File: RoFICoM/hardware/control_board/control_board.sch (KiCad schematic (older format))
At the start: 27 parts, among them J1 Skirt Cable, J2 M+, J3 M-, J4 SWD, J5 DBG_UART, J6 SYS_CON, J7 SLIDER, U1 STM32G071GBU6, U2 DRV8837C, U3 BU52272NUZ, U4 MIC5365, U5 BU52272NUZ

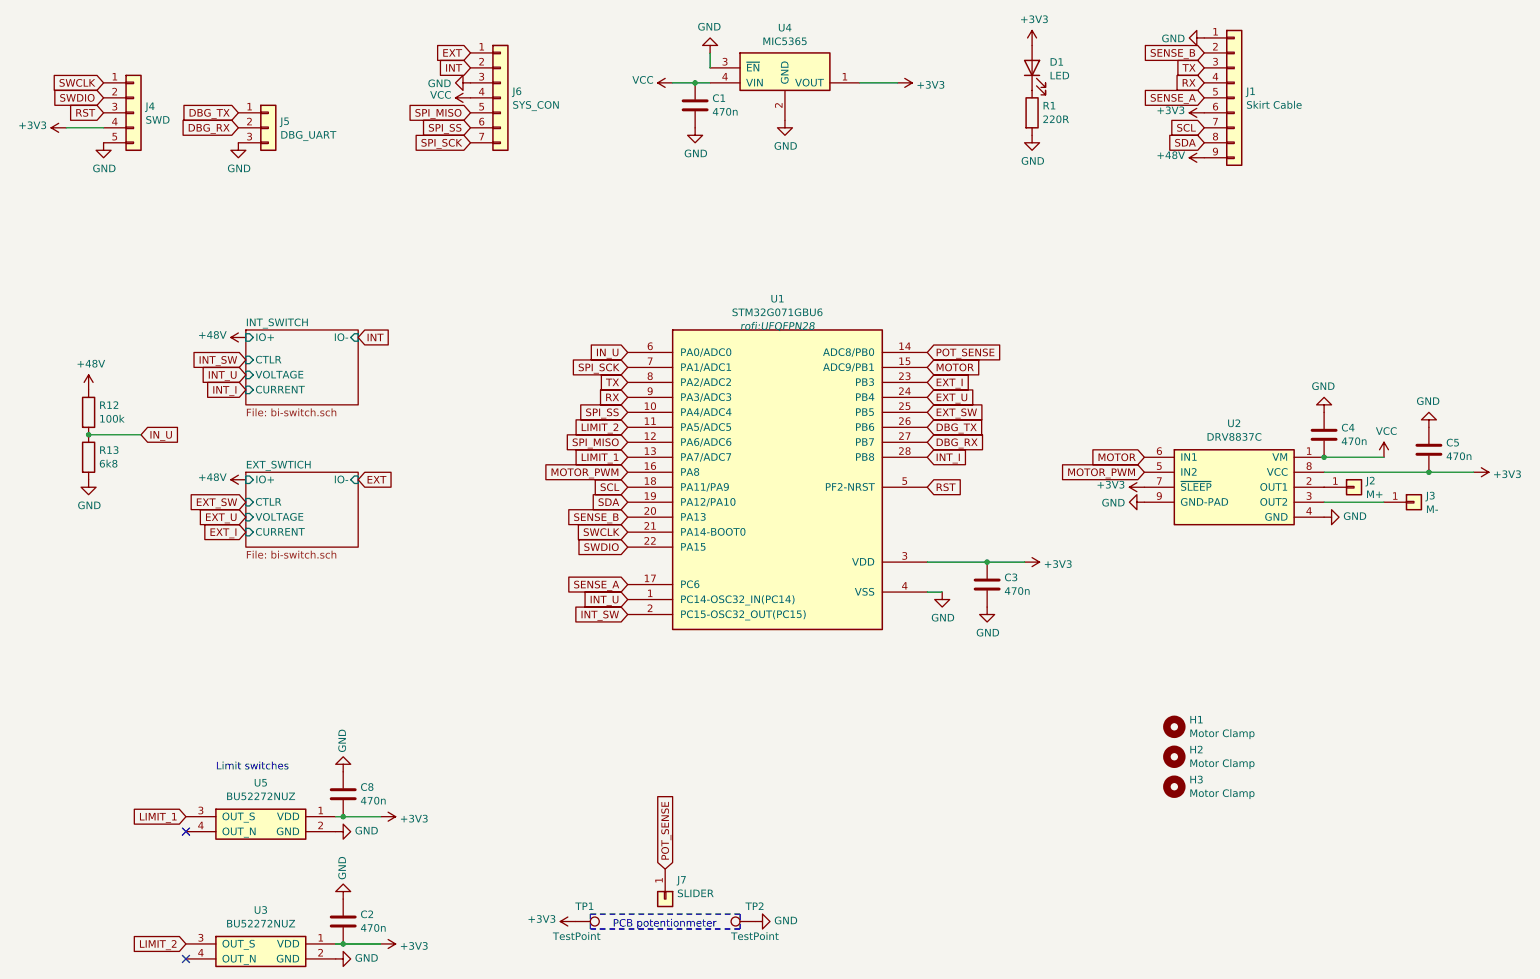
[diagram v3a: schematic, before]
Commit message: RoFICoM: Add new board revision
- change voltage regulator and switching transistors
- fix wrong wiring of SWD
- add Molex board-to-board connectors for system and debugging
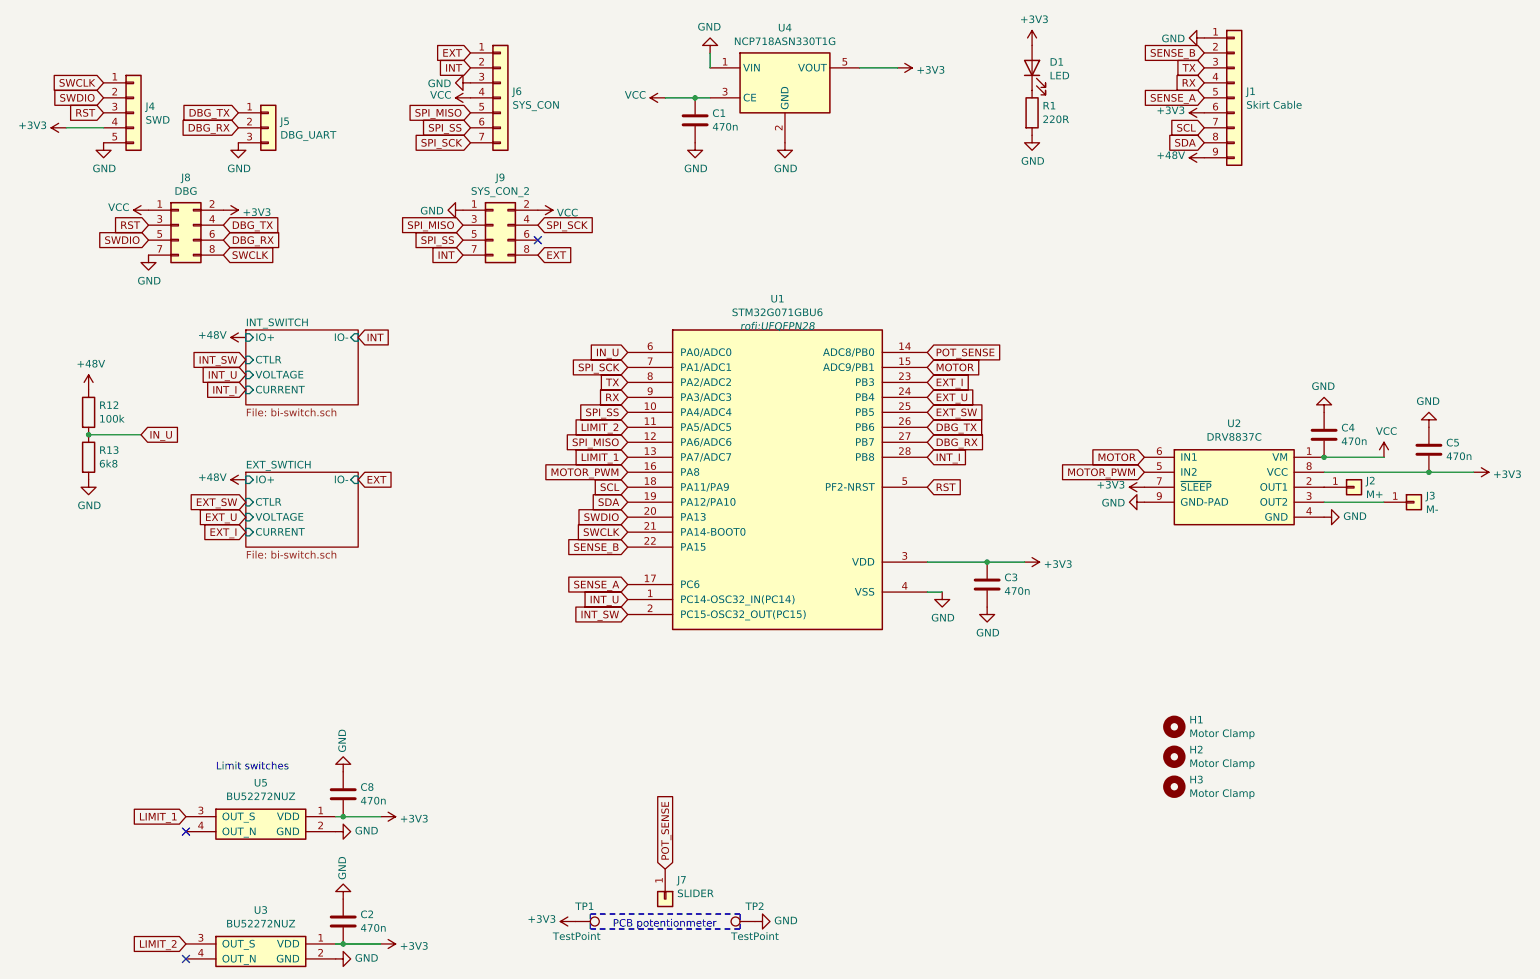
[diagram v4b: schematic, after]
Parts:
- removed U4: MIC5365, rofi:MLF-4, symbol rofi:MIC5365
- added J8: DBG, rofi:molex-505006-0812, symbol Connector_Generic:Conn_02x04_Odd_Even
- added J9: SYS_CON_2, rofi:molex-505006-0812, symbol Connector_Generic:Conn_02x04_Odd_Even
- added U4: NCP718ASN330T1G, Package_TO_SOT_SMD:SOT-23-5, symbol Regulator_Linear:XC6220B331MR
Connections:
- net +3V3: now also J8.2 (Pin_2), U4.5 (VOUT)
- net DBG_RX: now also J8.6 (Pin_6)
- net DBG_TX: now also J8.4 (Pin_4)
- net EXT: now also J9.8 (Pin_8)
- net GND: now also J8.7 (Pin_7), J9.1 (Pin_1), U4.1 (VIN), U4.2 (GND)
- net INT: now also J9.7 (Pin_7)
- net RST: now also J8.3 (Pin_3)
- net SENSE_B: now also U1.22 (PA15); no longer U1.20 (PA13)
- net SPI_MISO: now also J9.3 (Pin_3)
- net SPI_SCK: now also J9.4 (Pin_4)
- net SPI_SS: now also J9.5 (Pin_5)
- net SWCLK: now also J8.8 (Pin_8)
- net SWDIO: now also U1.20 (PA13), J8.5 (Pin_5); no longer U1.22 (PA15)
- net VCC: now also J8.1 (Pin_1), J9.2 (Pin_2), U4.3 (CE)
- no-connect marks 2 -> 3
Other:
- moved on the sheet: C1
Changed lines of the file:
@@
-	1    0    0    -1
-$EndComp
-$Comp
-L rofi:MIC5365 U4
-U 1 1 5C8FC8F0
-P 5750 1400
-F 0 "U4" H 5750 1767 50  0000 C CNN
-F 1 "MIC5365" H 5750 1676 50  0000 C CNN
-F 2 "rofi:MLF-4" H 5750 1400 50  0001 C CNN
-F 3 "" H 5750 1400 50  0001 C CNN
-F 4 "MIC5365-3.3YMT-TZ" H 0   0   50  0001 C CNN "manf#"
-	1    5750 1400
 	1    0    0    -1
 $EndComp
@@
 Text GLabel 4700 4400 0    50   Input ~ 0
 SWCLK
-Text GLabel 4700 4500 0    50   Input ~ 0
+Text GLabel 4700 4300 0    50   Input ~ 0
 SWDIO
 Text GLabel 6700 4100 2    50   Input ~ 0
@@
 L power:GND #PWR0104
 U 1 1 5C86B942
-P 5750 1650
-F 0 "#PWR0104" H 5750 1400 50  0001 C CNN
-F 1 "GND" H 5755 1477 50  0000 C CNN
-F 2 "" H 5750 1650 50  0001 C CNN
-F 3 "" H 5750 1650 50  0001 C CNN
-	1    5750 1650
+P 5750 1800
+F 0 "#PWR0104" H 5750 1550 50  0001 C CNN
+F 1 "GND" H 5755 1627 50  0000 C CNN
+F 2 "" H 5750 1800 50  0001 C CNN
+F 3 "" H 5750 1800 50  0001 C CNN
+	1    5750 1800
 	1    0    0    -1
 $EndComp
@@
 L power:VCC #PWR0106
 U 1 1 5C86BBA9
-P 5000 1400
-F 0 "#PWR0106" H 5000 1250 50  0001 C CNN
-F 1 "VCC" V 5018 1527 50  0000 L CNN
-F 2 "" H 5000 1400 50  0001 C CNN
-F 3 "" H 5000 1400 50  0001 C CNN
-	1    5000 1400
+P 4950 1500
+F 0 "#PWR0106" H 4950 1350 50  0001 C CNN
+F 1 "VCC" V 4968 1627 50  0000 L CNN
+F 2 "" H 4950 1500 50  0001 C CNN
+F 3 "" H 4950 1500 50  0001 C CNN
+	1    4950 1500
 	0    -1   -1   0
 $EndComp
@@
 L power:+3V3 #PWR0107
 U 1 1 5C86BC44
-P 6500 1400
-F 0 "#PWR0107" H 6500 1250 50  0001 C CNN
-F 1 "+3V3" V 6515 1528 50  0000 L CNN
-F 2 "" H 6500 1400 50  0001 C CNN
-F 3 "" H 6500 1400 50  0001 C CNN
-	1    6500 1400
+P 6500 1300
+F 0 "#PWR0107" H 6500 1150 50  0001 C CNN
+F 1 "+3V3" V 6515 1428 50  0000 L CNN
+F 2 "" H 6500 1300 50  0001 C CNN
+F 3 "" H 6500 1300 50  0001 C CNN
+	1    6500 1300
 	0    1    1    0
 $EndComp
@@
 	1    0    0    -1
 $EndComp
-Wire Wire Line
-	5000 1400 5150 1400
 $Comp
 L Device:C C1
 U 1 1 5C86BE43
-P 5150 1550
-F 0 "C1" H 5265 1596 50  0000 L CNN
-F 1 "470n" H 5265 1505 50  0000 L CNN
-F 2 "Capacitor_SMD:C_0402_1005Metric" H 5188 1400 50  0001 C CNN
-F 3 "~" H 5150 1550 50  0001 C CNN
-F 4 "CC0402ZRY5V6BB474" H 0   0   50  0001 C CNN "manf#"
-	1    5150 1550
-	1    0    0    -1
-$EndComp
-Connection ~ 5150 1400
-Wire Wire Line
-	5150 1400 5250 1400
+P 5150 1650
+F 0 "C1" H 5265 1696 50  0000 L CNN
+F 1 "470n" H 5265 1605 50  0000 L CNN
+F 2 "Capacitor_SMD:C_0402_1005Metric" H 5188 1500 50  0001 C CNN
+F 3 "~" H 5150 1650 50  0001 C CNN
+F 4 "CC0402ZRY5V6BB474" H 0   100 50  0001 C CNN "manf#"
+	1    5150 1650
+	1    0    0    -1
+$EndComp
 $Comp
 L power:GND #PWR0109
 U 1 1 5C86BE7F
-P 5150 1700
-F 0 "#PWR0109" H 5150 1450 50  0001 C CNN
-F 1 "GND" H 5155 1527 50  0000 C CNN
-F 2 "" H 5150 1700 50  0001 C CNN
-F 3 "" H 5150 1700 50  0001 C CNN
-	1    5150 1700
+P 5150 1800
+F 0 "#PWR0109" H 5150 1550 50  0001 C CNN
+F 1 "GND" H 5155 1627 50  0000 C CNN
+F 2 "" H 5150 1800 50  0001 C CNN
+F 3 "" H 5150 1800 50  0001 C CNN
+	1    5150 1800
 	1    0    0    -1
 $EndComp
@@
 Text GLabel 4700 4750 0    50   Input ~ 0
 SENSE_A
-Text GLabel 4700 4300 0    50   Input ~ 0
+Text GLabel 4700 4500 0    50   Input ~ 0
 SENSE_B
 Text GLabel 4700 3200 0    50   Input ~ 0
@@
 $EndComp
 Wire Wire Line
-	6250 1400 6500 1400
+	6250 1300 6500 1300
+Wire Wire Line
+	4950 1500 5150 1500
+Connection ~ 5150 1500
+Wire Wire Line
+	5150 1500 5250 1500
+$Comp
+L Connector_Generic:Conn_02x04_Odd_Even J9
+U 1 1 5D741CB4
+P 3800 2350
+F 0 "J9" H 3850 2667 50  0000 C CNN
+F 1 "SYS_CON_2" H 3850 2576 50  0000 C CNN
+F 2 "rofi:molex-505006-0812" H 3800 2350 50  0001 C CNN
+F 3 "~" H 3800 2350 50  0001 C CNN
+	1    3800 2350
+	1    0    0    -1
+$EndComp
+$Comp
+L power:GND #PWR0150
+U 1 1 5D74293A
+P 3600 2250
+F 0 "#PWR0150" H 3600 2000 50  0001 C CNN
+F 1 "GND" V 3605 2122 50  0000 R CNN
+F 2 "" H 3600 2250 50  0001 C CNN
+F 3 "" H 3600 2250 50  0001 C CNN
+	1    3600 2250
+	0    1    1    0
+$EndComp
+Text GLabel 4100 2550 2    50   Input ~ 0
+EXT
+Text GLabel 3600 2550 0    50   Input ~ 0
+INT
+$Comp
+L power:VCC #PWR0151
+U 1 1 5D743187
+P 4100 2250
+F 0 "#PWR0151" H 4100 2100 50  0001 C CNN
+F 1 "VCC" V 4118 2377 50  0000 L CNN
+F 2 "" H 4100 2250 50  0001 C CNN
+F 3 "" H 4100 2250 50  0001 C CNN
+	1    4100 2250
+	0    1    1    0
+$EndComp
+Text GLabel 3600 2350 0    50   Input ~ 0
+SPI_MISO
+Text GLabel 3600 2450 0    50   Input ~ 0
+SPI_SS
+Text GLabel 4100 2350 2    50   Input ~ 0
+SPI_SCK
+NoConn ~ 4100 2450
+$Comp
+L Connector_Generic:Conn_02x04_Odd_Even J8
+U 1 1 5D752682
+P 1700 2350
+F 0 "J8" H 1750 2667 50  0000 C CNN
+F 1 "DBG" H 1750 2576 50  0000 C CNN
+F 2 "rofi:molex-505006-0812" H 1700 2350 50  0001 C CNN
+F 3 "~" H 1700 2350 50  0001 C CNN
+	1    1700 2350
+	1    0    0    -1
+$EndComp
+$Comp
+L power:GND #PWR0152
+U 1 1 5D753C01
+P 1500 2550
+F 0 "#PWR0152" H 1500 2300 50  0001 C CNN
+F 1 "GND" H 1505 2377 50  0000 C CNN
+F 2 "" H 1500 2550 50  0001 C CNN
+F 3 "" H 1500 2550 50  0001 C CNN
+	1    1500 2550
+	1    0    0    -1
+$EndComp
+$Comp
+L power:+3V3 #PWR0153
+U 1 1 5D753F95
+P 2000 2250
+F 0 "#PWR0153" H 2000 2100 50  0001 C CNN
+F 1 "+3V3" V 2015 2378 50  0000 L CNN
+F 2 "" H 2000 2250 50  0001 C CNN
+F 3 "" H 2000 2250 50  0001 C CNN
+	1    2000 2250
+	0    1    1    0
+$EndComp
+Text GLabel 2000 2550 2    50   Input ~ 0
+SWCLK
+Text GLabel 2000 2450 2    50   Input ~ 0
+DBG_RX
+Text GLabel 2000 2350 2    50   Input ~ 0
+DBG_TX
+$Comp
+L power:VCC #PWR0154
+U 1 1 5D756A68
+P 1500 2250
+F 0 "#PWR0154" H 1500 2100 50  0001 C CNN
+F 1 "VCC" V 1518 2377 50  0000 L CNN
+F 2 "" H 1500 2250 50  0001 C CNN
+F 3 "" H 1500 2250 50  0001 C CNN
+	1    1500 2250
+	0    -1   -1   0
+$EndComp
+$Comp
+L Regulator_Linear:XC6220B331MR U4
+U 1 1 5D78320C
+P 5750 1400
+F 0 "U4" H 5750 1767 50  0000 C CNN
+F 1 "NCP718ASN330T1G" H 5750 1676 50  0000 C CNN
+F 2 "Package_TO_SOT_SMD:SOT-23-5" H 5750 1400 50  0001 C CNN
+F 3 "https://www.torexsemi.com/file/xc6220/XC6220.pdf" H 6500 400 50  0001 C CNN
+F 4 "NCP718ASN330T1G" H 5750 1400 50  0001 C CNN "manf#"
+	1    5750 1400
+	1    0    0    -1
+$EndComp
+Text GLabel 1500 2450 0    50   Input ~ 0
+SWDIO
+Text GLabel 1500 2350 0    50   Input ~ 0
+RST
 $EndSCHEMATC

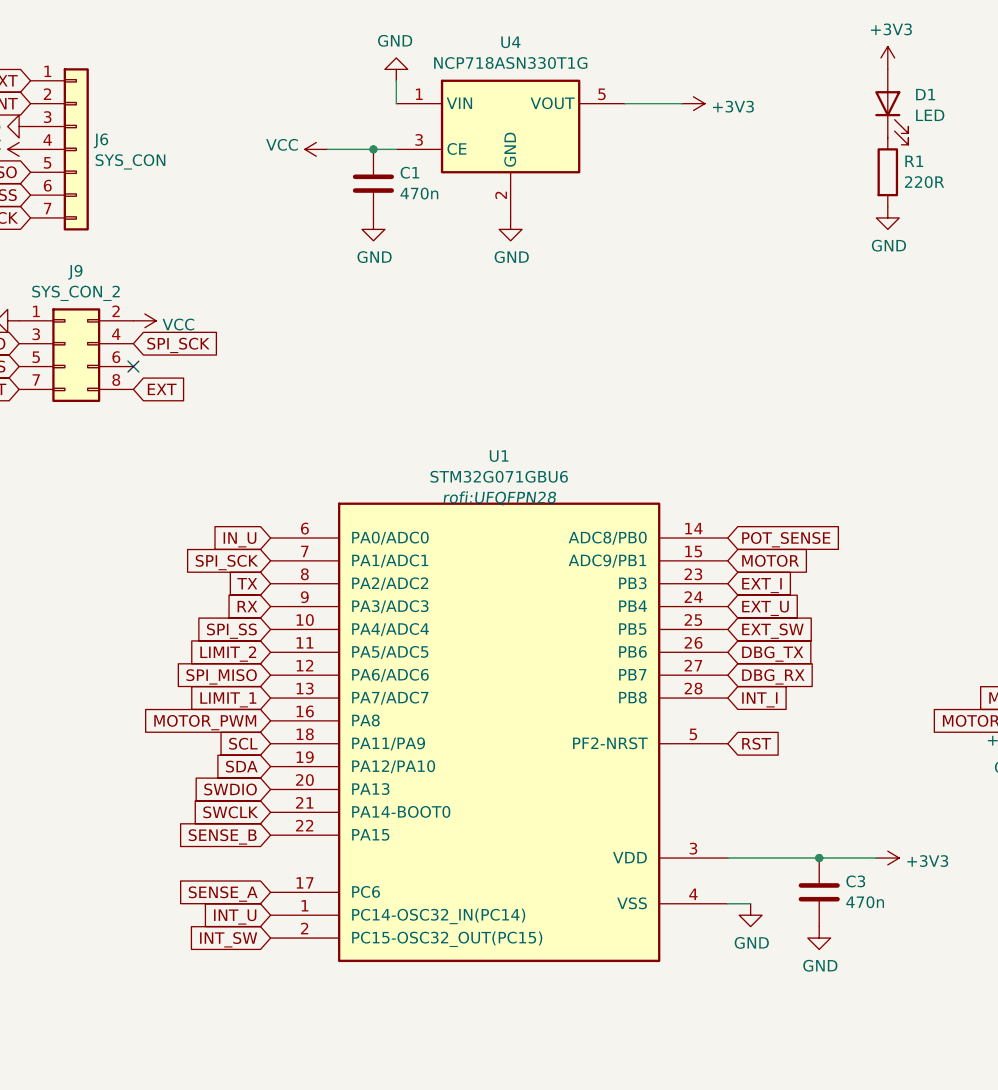
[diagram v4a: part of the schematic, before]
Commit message: RoFICoM: Fix bugs of v0.4 and introduce v0.5
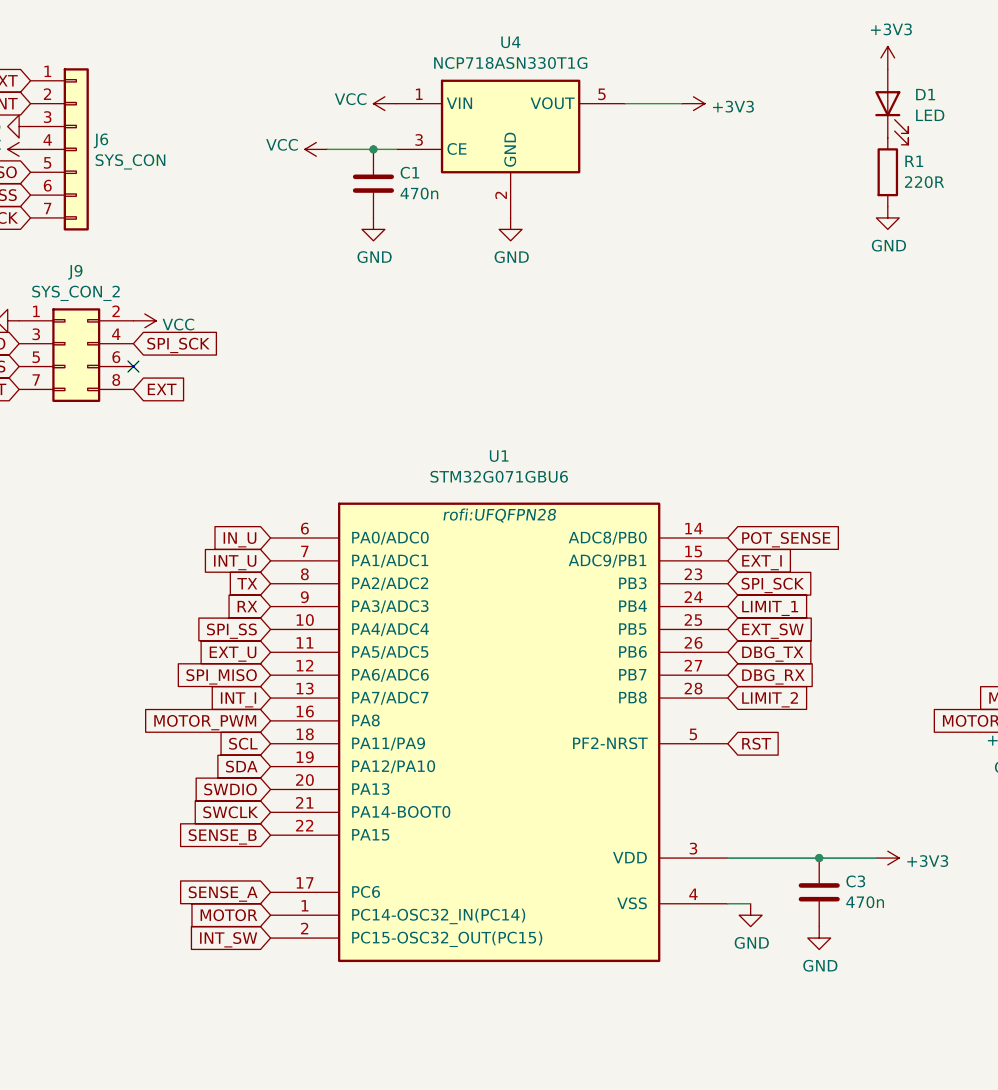
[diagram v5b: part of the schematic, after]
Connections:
- net EXT_I: now also U1.15 (ADC9/PB1); no longer U1.23 (PB3)
- net EXT_U: now also U1.11 (PA5/ADC5); no longer U1.24 (PB4)
- net GND: no longer U4.1 (VIN)
- net INT_I: now also U1.13 (PA7/ADC7); no longer U1.28 (PB8)
- net INT_U: now also U1.7 (PA1/ADC1); no longer U1.1 (PC14-OSC32_IN(PC14))
- net LIMIT_1: now also U1.24 (PB4); no longer U1.13 (PA7/ADC7)
- net LIMIT_2: now also U1.28 (PB8); no longer U1.11 (PA5/ADC5)
- net MOTOR: now also U1.1 (PC14-OSC32_IN(PC14)); no longer U1.15 (ADC9/PB1)
- net SPI_SCK: now also U1.23 (PB3); no longer U1.7 (PA1/ADC1)
- net VCC: now also U4.1 (VIN)
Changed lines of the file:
@@
 EESchema Schematic File Version 4
-LIBS:control_board-cache
-EELAYER 29 0
+EELAYER 30 0
 EELAYER END
 $Descr A4 11693 8268
@@
 F 0 "U1" H 5700 5257 50  0000 C CNN
 F 1 "STM32G071GBU6" H 5700 5166 50  0000 C CNN
-F 2 "rofi:UFQFPN28" H 5700 5075 50  0000 C CIN
+F 2 "rofi:UFQFPN28" H 5700 5000 50  0000 C CIN
 F 3 "" H 5700 3100 50  0000 C CNN
 F 4 "STM32G071GBU6" H 5700 4050 50  0001 C CNN "manf#"
@@
 Text GLabel 4700 4100 0    50   Input ~ 0
 SCL
-Text GLabel 4700 3300 0    50   Input ~ 0
+Text GLabel 6700 3400 2    50   Input ~ 0
 SPI_SCK
 Text GLabel 4700 3600 0    50   Input ~ 0
@@
 Text GLabel 4700 4000 0    50   Input ~ 0
 MOTOR_PWM
-Text GLabel 6700 3300 2    50   Input ~ 0
+Text GLabel 4700 4850 0    50   Input ~ 0
 MOTOR
 Wire Wire Line
@@
 $EndComp
 $Comp
-L power:GND #PWR0105
-U 1 1 5C86B95E
-P 5250 1200
-F 0 "#PWR0105" H 5250 950 50  0001 C CNN
-F 1 "GND" H 5255 1027 50  0000 C CNN
-F 2 "" H 5250 1200 50  0001 C CNN
-F 3 "" H 5250 1200 50  0001 C CNN
-	1    5250 1200
-	-1   0    0    1
-$EndComp
-Wire Wire Line
-	5250 1200 5250 1300
-$Comp
 L power:VCC #PWR0106
 U 1 1 5C86BBA9
@@
 NoConn ~ 1750 6400
 NoConn ~ 1750 7250
-Text GLabel 4700 3900 0    50   Input ~ 0
+Text GLabel 6700 3500 2    50   Input ~ 0
 LIMIT_1
-Text GLabel 4700 3700 0    50   Input ~ 0
+Text GLabel 6700 3900 2    50   Input ~ 0
 LIMIT_2
 Text GLabel 6700 3200 2    50   Input ~ 0
@@
 Text GLabel 4700 4950 0    50   Input ~ 0
 INT_SW
-Text GLabel 4700 4850 0    50   Input ~ 0
+Text GLabel 4700 3300 0    50   Input ~ 0
 INT_U
-Text GLabel 6700 3900 2    50   Input ~ 0
+Text GLabel 4700 3900 0    50   Input ~ 0
 INT_I
 Text GLabel 6700 3600 2    50   Input ~ 0
 EXT_SW
-Text GLabel 6700 3500 2    50   Input ~ 0
+Text GLabel 4700 3700 0    50   Input ~ 0
 EXT_U
-Text GLabel 6700 3400 2    50   Input ~ 0
+Text GLabel 6700 3300 2    50   Input ~ 0
 EXT_I
 Text GLabel 4700 4750 0    50   Input ~ 0
@@
 Text GLabel 1500 2350 0    50   Input ~ 0
 RST
+$Comp
+L power:VCC #PWR0105
+U 1 1 5F468B95
+P 5250 1300
+F 0 "#PWR0105" H 5250 1150 50  0001 C CNN
+F 1 "VCC" V 5268 1427 50  0000 L CNN
+F 2 "" H 5250 1300 50  0001 C CNN
+F 3 "" H 5250 1300 50  0001 C CNN
+	1    5250 1300
+	0    -1   -1   0
+$EndComp
 $EndSCHEMATC
